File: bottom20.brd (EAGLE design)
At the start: 160 x 100 mm, 0 parts

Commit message: + bot.sch (Module verknüpfen + Anschluss)
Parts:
- added 5V-SCHALTREGLER1:C3: 100uF, 16V, ±20 %, iceberg20:CAPACITOR-THT-6.3
- added 5V-SCHALTREGLER1:C4: 1000uF, 25V, ±20 %, iceberg20:CAPACITOR-THT-10
- added 5V-SCHALTREGLER1:D1: 1N5822, iceberg20:DO-201AD
- added 5V-SCHALTREGLER1:IC2: LM2576, iceberg20:TO220-5PIN
- added 5V-SCHALTREGLER1:L1: L-100U, iceberg20:PISR
- added 5V-SCHALTREGLER1:R1: 100k, iceberg20:R0805
- added ANSCHLUSS1:CON1: Interface, iceberg20:CON-01X03
- added ANSCHLUSS1:X1: FTDI-Adapter, iceberg20:PIN-HEADER-ANGLED-6
- added ARDUINO1:C1, ARDUINO1:C5: 100nF, iceberg20:C0805
- added ARDUINO1:C2, ARDUINO1:C4: 1uF, iceberg20:C0805
- added ARDUINO1:C3: 4,7 µF, 16 V, ±20%, 3x5 mm, iceberg20:CAPACITOR-THT-3
- added ARDUINO1:IC1: ATMEGA328P-AU, iceberg20:ATMEGA328P-AU
- added ARDUINO1:Q1: 16MHz, iceberg20:CRYSTAL_HC49U-V
- added ARDUINO1:R1, ARDUINO1:R2: 1K, iceberg20:R0805
- added ARDUINO1:TP1: SCK, iceberg20:TESTPAD_B2,54
- added ARDUINO1:TP2: MISO, iceberg20:TESTPAD_B2,54
- added ARDUINO1:TP3: MOSI, iceberg20:TESTPAD_B2,54
- added ARDUINO1:TP4: SS, iceberg20:TESTPAD_B2,54
- added LED1:LED1, LED1:LED10, LED1:LED11, LED1:LED12, LED1:LED13, LED1:LED14, LED1:LED15, LED1:LED16, LED1:LED17, LED1:LED18, LED1:LED19, LED1:LED2, LED1:LED20, LED1:LED21, LED1:LED22, LED1:LED23, LED1:LED24, LED1:LED25, LED1:LED26, LED1:LED27, LED1:LED28, LED1:LED29, LED1:LED3, LED1:LED30, LED1:LED31, LED1:LED32, LED1:LED4, LED1:LED5, LED1:LED6, LED1:LED7, LED1:LED8, LED1:LED9: WS2812B, iceberg20:5050
- added PHOTOTRANSISTOR1:IC1, PHOTOTRANSISTOR2:IC1: MULTIPLEXER, iceberg20:SO24
- added PHOTOTRANSISTOR1:R1, PHOTOTRANSISTOR1:R10, PHOTOTRANSISTOR1:R11, PHOTOTRANSISTOR1:R12, PHOTOTRANSISTOR1:R13, PHOTOTRANSISTOR1:R14, PHOTOTRANSISTOR1:R15, PHOTOTRANSISTOR1:R16, PHOTOTRANSISTOR1:R2, PHOTOTRANSISTOR1:R3, PHOTOTRANSISTOR1:R4, PHOTOTRANSISTOR1:R5, PHOTOTRANSISTOR1:R6, PHOTOTRANSISTOR1:R7, PHOTOTRANSISTOR1:R8, PHOTOTRANSISTOR1:R9, PHOTOTRANSISTOR2:R1, PHOTOTRANSISTOR2:R10, PHOTOTRANSISTOR2:R11, PHOTOTRANSISTOR2:R12, PHOTOTRANSISTOR2:R13, PHOTOTRANSISTOR2:R14, PHOTOTRANSISTOR2:R15, PHOTOTRANSISTOR2:R16, PHOTOTRANSISTOR2:R2, PHOTOTRANSISTOR2:R3, PHOTOTRANSISTOR2:R4, PHOTOTRANSISTOR2:R5, PHOTOTRANSISTOR2:R6, PHOTOTRANSISTOR2:R7, PHOTOTRANSISTOR2:R8, PHOTOTRANSISTOR2:R9: R, iceberg20:R0805
- added PHOTOTRANSISTOR1:T1, PHOTOTRANSISTOR1:T10, PHOTOTRANSISTOR1:T11, PHOTOTRANSISTOR1:T12, PHOTOTRANSISTOR1:T13, PHOTOTRANSISTOR1:T14, PHOTOTRANSISTOR1:T15, PHOTOTRANSISTOR1:T16, PHOTOTRANSISTOR1:T2, PHOTOTRANSISTOR1:T3, PHOTOTRANSISTOR1:T4, PHOTOTRANSISTOR1:T5, PHOTOTRANSISTOR1:T6, PHOTOTRANSISTOR1:T7, PHOTOTRANSISTOR1:T8, PHOTOTRANSISTOR1:T9, PHOTOTRANSISTOR2:T1, PHOTOTRANSISTOR2:T10, PHOTOTRANSISTOR2:T11, PHOTOTRANSISTOR2:T12, PHOTOTRANSISTOR2:T13, PHOTOTRANSISTOR2:T14, PHOTOTRANSISTOR2:T15, PHOTOTRANSISTOR2:T16, PHOTOTRANSISTOR2:T2, PHOTOTRANSISTOR2:T3, PHOTOTRANSISTOR2:T4, PHOTOTRANSISTOR2:T5, PHOTOTRANSISTOR2:T6, PHOTOTRANSISTOR2:T7, PHOTOTRANSISTOR2:T8, PHOTOTRANSISTOR2:T9: SFH320, iceberg20:PLCC-2
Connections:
- new net +12V: 5V-SCHALTREGLER1:C3.1, 5V-SCHALTREGLER1:IC2.1, ANSCHLUSS1:CON1.3
- new net +5V: 5V-SCHALTREGLER1:C4.1, 5V-SCHALTREGLER1:IC2.4, 5V-SCHALTREGLER1:L1.2, 5V-SCHALTREGLER1:R1.2, ARDUINO1:C2.1, ARDUINO1:C3.1, ARDUINO1:C4.1, ARDUINO1:IC1.18, ARDUINO1:IC1.4, ARDUINO1:IC1.6, LED1:LED1.VDD, LED1:LED10.VDD, LED1:LED11.VDD, LED1:LED12.VDD, LED1:LED13.VDD, LED1:LED14.VDD, LED1:LED15.VDD, LED1:LED16.VDD, LED1:LED17.VDD, LED1:LED18.VDD, LED1:LED19.VDD, LED1:LED2.VDD, LED1:LED20.VDD, LED1:LED21.VDD, LED1:LED22.VDD, LED1:LED23.VDD, LED1:LED24.VDD, LED1:LED25.VDD, LED1:LED26.VDD, LED1:LED27.VDD, LED1:LED28.VDD, LED1:LED29.VDD, LED1:LED3.VDD, LED1:LED30.VDD, LED1:LED31.VDD, LED1:LED32.VDD, LED1:LED4.VDD, LED1:LED5.VDD, LED1:LED6.VDD, LED1:LED7.VDD, LED1:LED8.VDD, LED1:LED9.VDD, PHOTOTRANSISTOR1:IC1.24, PHOTOTRANSISTOR1:R1.2, PHOTOTRANSISTOR1:R10.2, PHOTOTRANSISTOR1:R11.2, PHOTOTRANSISTOR1:R12.2, PHOTOTRANSISTOR1:R13.2, PHOTOTRANSISTOR1:R14.2, PHOTOTRANSISTOR1:R15.2, PHOTOTRANSISTOR1:R16.2, PHOTOTRANSISTOR1:R2.2, PHOTOTRANSISTOR1:R3.2, PHOTOTRANSISTOR1:R4.2, PHOTOTRANSISTOR1:R5.2, PHOTOTRANSISTOR1:R6.2, PHOTOTRANSISTOR1:R7.2, PHOTOTRANSISTOR1:R8.2, PHOTOTRANSISTOR1:R9.2, PHOTOTRANSISTOR2:IC1.24, PHOTOTRANSISTOR2:R1.2, PHOTOTRANSISTOR2:R10.2, PHOTOTRANSISTOR2:R11.2, PHOTOTRANSISTOR2:R12.2, PHOTOTRANSISTOR2:R13.2, PHOTOTRANSISTOR2:R14.2, PHOTOTRANSISTOR2:R15.2, PHOTOTRANSISTOR2:R16.2, PHOTOTRANSISTOR2:R2.2, PHOTOTRANSISTOR2:R3.2, PHOTOTRANSISTOR2:R4.2, PHOTOTRANSISTOR2:R5.2, PHOTOTRANSISTOR2:R6.2, PHOTOTRANSISTOR2:R7.2, PHOTOTRANSISTOR2:R8.2, PHOTOTRANSISTOR2:R9.2
- new net 5V-SCHALTREGLER1:N$1: 5V-SCHALTREGLER1:IC2.5, 5V-SCHALTREGLER1:R1.1
- new net 5V-SCHALTREGLER1:N$2: 5V-SCHALTREGLER1:D1.1, 5V-SCHALTREGLER1:IC2.2, 5V-SCHALTREGLER1:L1.1
- new net ANSCHLUSS1:CTS: ANSCHLUSS1:X1.P$2
- new net ANSCHLUSS1:DTR: ANSCHLUSS1:X1.P$6
- new net ANSCHLUSS1:RX: ANSCHLUSS1:X1.P$5
- new net ANSCHLUSS1:TX: ANSCHLUSS1:X1.P$4
- new net ARDUINO1:A1: ARDUINO1:IC1.24
- new net ARDUINO1:A2: ARDUINO1:IC1.25
- new net ARDUINO1:A3: ARDUINO1:IC1.26
- new net ARDUINO1:ADC6: ARDUINO1:IC1.19
- new net ARDUINO1:ADC7: ARDUINO1:IC1.22
- new net ARDUINO1:AIN0: ARDUINO1:IC1.10
- new net ARDUINO1:AIN1: ARDUINO1:IC1.11
- new net ARDUINO1:AO: ARDUINO1:IC1.23
- new net ARDUINO1:ARDUINO-RESET: ARDUINO1:C1.1
- new net ARDUINO1:D10: ARDUINO1:IC1.14, ARDUINO1:TP4.TP
- new net ARDUINO1:D4: ARDUINO1:IC1.2
- new net ARDUINO1:D5: ARDUINO1:IC1.9
- new net ARDUINO1:D8: ARDUINO1:IC1.12
- new net ARDUINO1:D9: ARDUINO1:IC1.13
- new net ARDUINO1:INT0: ARDUINO1:IC1.1
- new net ARDUINO1:INT1: ARDUINO1:IC1.32
- new net ARDUINO1:N$1: ARDUINO1:C1.2, ARDUINO1:IC1.29
- new net ARDUINO1:N$12: ARDUINO1:IC1.30, ARDUINO1:R1.1
- new net ARDUINO1:N$13: ARDUINO1:IC1.31, ARDUINO1:R2.1
- new net ARDUINO1:N$5: ARDUINO1:IC1.15, ARDUINO1:TP3.TP
- new net ARDUINO1:N$6: ARDUINO1:IC1.16, ARDUINO1:TP2.TP
- new net ARDUINO1:N$7: ARDUINO1:IC1.17, ARDUINO1:TP1.TP
- new net ARDUINO1:N$8: ARDUINO1:C5.1, ARDUINO1:IC1.20
- new net ARDUINO1:SCL: ARDUINO1:IC1.28
- new net ARDUINO1:SDA: ARDUINO1:IC1.27
- new net GND: 5V-SCHALTREGLER1:C3.2, 5V-SCHALTREGLER1:C4.2, 5V-SCHALTREGLER1:D1.2, 5V-SCHALTREGLER1:IC2.3, ANSCHLUSS1:X1.P$1, ARDUINO1:C2.2, ARDUINO1:C3.2, ARDUINO1:C4.2, ARDUINO1:C5.2, ARDUINO1:IC1.21, ARDUINO1:IC1.3, ARDUINO1:IC1.5, ARDUINO1:IC1.7, ARDUINO1:IC1.8, ARDUINO1:Q1.1, ARDUINO1:Q1.2, LED1:LED1.GND, LED1:LED10.GND, LED1:LED11.GND, LED1:LED12.GND, LED1:LED13.GND, LED1:LED14.GND, LED1:LED15.GND, LED1:LED16.GND, LED1:LED17.GND, LED1:LED18.GND, LED1:LED19.GND, LED1:LED2.GND, LED1:LED20.GND, LED1:LED21.GND, LED1:LED22.GND, LED1:LED23.GND, LED1:LED24.GND, LED1:LED25.GND, LED1:LED26.GND, LED1:LED27.GND, LED1:LED28.GND, LED1:LED29.GND, LED1:LED3.GND, LED1:LED30.GND, LED1:LED31.GND, LED1:LED32.GND, LED1:LED4.GND, LED1:LED5.GND, LED1:LED6.GND, LED1:LED7.GND, LED1:LED8.GND, LED1:LED9.GND
- new net LED-IN: LED1:LED1.IN
- new net LED1:CON-1: LED1:LED8.OUT, LED1:LED9.IN
- new net LED1:CON-2: LED1:LED16.OUT, LED1:LED17.IN
- new net LED1:CON-3: LED1:LED24.OUT, LED1:LED25.IN
- new net LED1:LED-IN1: LED1:LED2.OUT, LED1:LED3.IN
- new net LED1:LED-IN10: LED1:LED20.OUT, LED1:LED21.IN
- new net LED1:LED-IN11: LED1:LED22.OUT, LED1:LED23.IN
- new net LED1:LED-IN12: LED1:LED30.OUT, LED1:LED31.IN
- new net LED1:LED-IN2: LED1:LED4.OUT, LED1:LED5.IN
- new net LED1:LED-IN3: LED1:LED6.OUT, LED1:LED7.IN
- new net LED1:LED-IN4: LED1:LED26.OUT, LED1:LED27.IN
- new net LED1:LED-IN5: LED1:LED10.OUT, LED1:LED11.IN
- new net LED1:LED-IN6: LED1:LED12.OUT, LED1:LED13.IN
- new net LED1:LED-IN7: LED1:LED14.OUT, LED1:LED15.IN
- new net LED1:LED-IN8: LED1:LED28.OUT, LED1:LED29.IN
- new net LED1:LED-IN9: LED1:LED18.OUT, LED1:LED19.IN
- new net LED1:N$1: LED1:LED3.OUT, LED1:LED4.IN
- new net LED1:N$11: LED1:LED11.OUT, LED1:LED12.IN
- new net LED1:N$12: LED1:LED13.OUT, LED1:LED14.IN
- new net LED1:N$13: LED1:LED15.OUT, LED1:LED16.IN
- new net LED1:N$14: LED1:LED17.OUT, LED1:LED18.IN
- new net LED1:N$16: LED1:LED19.OUT, LED1:LED20.IN
- new net LED1:N$17: LED1:LED21.OUT, LED1:LED22.IN
- new net LED1:N$18: LED1:LED23.OUT, LED1:LED24.IN
- new net LED1:N$2: LED1:LED1.OUT, LED1:LED2.IN
- new net LED1:N$3: LED1:LED25.OUT, LED1:LED26.IN
- new net LED1:N$4: LED1:LED5.OUT, LED1:LED6.IN
- new net LED1:N$5: LED1:LED27.OUT, LED1:LED28.IN
- new net LED1:N$6: LED1:LED29.OUT, LED1:LED30.IN
- new net LED1:N$7: LED1:LED7.OUT, LED1:LED8.IN
- new net LED1:N$8: LED1:LED31.OUT, LED1:LED32.IN
- new net LED1:N$9: LED1:LED10.IN, LED1:LED9.OUT
- new net N$2: ANSCHLUSS1:CON1.2, ARDUINO1:R1.2
- new net N$3: ANSCHLUSS1:CON1.1, ARDUINO1:R2.2
- new net N$6: ANSCHLUSS1:X1.P$3
- new net PHOTOTRANSISTOR1:BIT0: PHOTOTRANSISTOR1:IC1.11
- new net PHOTOTRANSISTOR1:BIT1: PHOTOTRANSISTOR1:IC1.10
- new net PHOTOTRANSISTOR1:BIT2: PHOTOTRANSISTOR1:IC1.14
- new net PHOTOTRANSISTOR1:BIT3: PHOTOTRANSISTOR1:IC1.13
- new net PHOTOTRANSISTOR1:GND: PHOTOTRANSISTOR1:IC1.12, PHOTOTRANSISTOR1:T1.C, PHOTOTRANSISTOR1:T10.C, PHOTOTRANSISTOR1:T11.C, PHOTOTRANSISTOR1:T12.C, PHOTOTRANSISTOR1:T13.C, PHOTOTRANSISTOR1:T14.C, PHOTOTRANSISTOR1:T15.C, PHOTOTRANSISTOR1:T16.C, PHOTOTRANSISTOR1:T2.C, PHOTOTRANSISTOR1:T3.C, PHOTOTRANSISTOR1:T4.C, PHOTOTRANSISTOR1:T5.C, PHOTOTRANSISTOR1:T6.C, PHOTOTRANSISTOR1:T7.C, PHOTOTRANSISTOR1:T8.C, PHOTOTRANSISTOR1:T9.C
- new net PHOTOTRANSISTOR1:MULTIPLEXER-ENABLE: PHOTOTRANSISTOR1:IC1.15
- new net PHOTOTRANSISTOR1:N$1: PHOTOTRANSISTOR1:IC1.9, PHOTOTRANSISTOR1:R1.1, PHOTOTRANSISTOR1:T1.A
- new net PHOTOTRANSISTOR1:N$10: PHOTOTRANSISTOR1:IC1.3, PHOTOTRANSISTOR1:R7.1, PHOTOTRANSISTOR1:T7.A
- new net PHOTOTRANSISTOR1:N$11: PHOTOTRANSISTOR1:IC1.4, PHOTOTRANSISTOR1:R6.1, PHOTOTRANSISTOR1:T6.A
- new net PHOTOTRANSISTOR1:N$12: PHOTOTRANSISTOR1:IC1.17, PHOTOTRANSISTOR1:R10.1, PHOTOTRANSISTOR1:T10.A
- new net PHOTOTRANSISTOR1:N$14: PHOTOTRANSISTOR1:IC1.18, PHOTOTRANSISTOR1:R11.1, PHOTOTRANSISTOR1:T11.A
- new net PHOTOTRANSISTOR1:N$18: PHOTOTRANSISTOR1:IC1.20, PHOTOTRANSISTOR1:R13.1, PHOTOTRANSISTOR1:T13.A
- new net PHOTOTRANSISTOR1:N$2: PHOTOTRANSISTOR1:IC1.8, PHOTOTRANSISTOR1:R2.1, PHOTOTRANSISTOR1:T2.A
- new net PHOTOTRANSISTOR1:N$20: PHOTOTRANSISTOR1:IC1.21, PHOTOTRANSISTOR1:R14.1, PHOTOTRANSISTOR1:T14.A
- new net PHOTOTRANSISTOR1:N$22: PHOTOTRANSISTOR1:IC1.22, PHOTOTRANSISTOR1:R15.1, PHOTOTRANSISTOR1:T15.A
- new net PHOTOTRANSISTOR1:N$25: PHOTOTRANSISTOR1:IC1.23, PHOTOTRANSISTOR1:R16.1, PHOTOTRANSISTOR1:T16.A
- new net PHOTOTRANSISTOR1:N$26: PHOTOTRANSISTOR1:IC1.19, PHOTOTRANSISTOR1:R12.1, PHOTOTRANSISTOR1:T12.A
- new net PHOTOTRANSISTOR1:N$3: PHOTOTRANSISTOR1:IC1.7, PHOTOTRANSISTOR1:R3.1, PHOTOTRANSISTOR1:T3.A
- new net PHOTOTRANSISTOR1:N$4: PHOTOTRANSISTOR1:IC1.6, PHOTOTRANSISTOR1:R4.1, PHOTOTRANSISTOR1:T4.A
- new net PHOTOTRANSISTOR1:N$5: PHOTOTRANSISTOR1:IC1.5, PHOTOTRANSISTOR1:R5.1, PHOTOTRANSISTOR1:T5.A
- new net PHOTOTRANSISTOR1:N$7: PHOTOTRANSISTOR1:IC1.16, PHOTOTRANSISTOR1:R9.1, PHOTOTRANSISTOR1:T9.A
- new net PHOTOTRANSISTOR1:N$9: PHOTOTRANSISTOR1:IC1.2, PHOTOTRANSISTOR1:R8.1, PHOTOTRANSISTOR1:T8.A
- new net PHOTOTRANSISTOR1:TRANSISTOR-SIGNAL: PHOTOTRANSISTOR1:IC1.1
- new net PHOTOTRANSISTOR2:BIT0: PHOTOTRANSISTOR2:IC1.11
- new net PHOTOTRANSISTOR2:BIT1: PHOTOTRANSISTOR2:IC1.10
- new net PHOTOTRANSISTOR2:BIT2: PHOTOTRANSISTOR2:IC1.14
- new net PHOTOTRANSISTOR2:BIT3: PHOTOTRANSISTOR2:IC1.13
- new net PHOTOTRANSISTOR2:GND: PHOTOTRANSISTOR2:IC1.12, PHOTOTRANSISTOR2:T1.C, PHOTOTRANSISTOR2:T10.C, PHOTOTRANSISTOR2:T11.C, PHOTOTRANSISTOR2:T12.C, PHOTOTRANSISTOR2:T13.C, PHOTOTRANSISTOR2:T14.C, PHOTOTRANSISTOR2:T15.C, PHOTOTRANSISTOR2:T16.C, PHOTOTRANSISTOR2:T2.C, PHOTOTRANSISTOR2:T3.C, PHOTOTRANSISTOR2:T4.C, PHOTOTRANSISTOR2:T5.C, PHOTOTRANSISTOR2:T6.C, PHOTOTRANSISTOR2:T7.C, PHOTOTRANSISTOR2:T8.C, PHOTOTRANSISTOR2:T9.C
- new net PHOTOTRANSISTOR2:MULTIPLEXER-ENABLE: PHOTOTRANSISTOR2:IC1.15
- new net PHOTOTRANSISTOR2:N$1: PHOTOTRANSISTOR2:IC1.9, PHOTOTRANSISTOR2:R1.1, PHOTOTRANSISTOR2:T1.A
- new net PHOTOTRANSISTOR2:N$10: PHOTOTRANSISTOR2:IC1.3, PHOTOTRANSISTOR2:R7.1, PHOTOTRANSISTOR2:T7.A
- new net PHOTOTRANSISTOR2:N$11: PHOTOTRANSISTOR2:IC1.4, PHOTOTRANSISTOR2:R6.1, PHOTOTRANSISTOR2:T6.A
- new net PHOTOTRANSISTOR2:N$12: PHOTOTRANSISTOR2:IC1.17, PHOTOTRANSISTOR2:R10.1, PHOTOTRANSISTOR2:T10.A
- new net PHOTOTRANSISTOR2:N$14: PHOTOTRANSISTOR2:IC1.18, PHOTOTRANSISTOR2:R11.1, PHOTOTRANSISTOR2:T11.A
- new net PHOTOTRANSISTOR2:N$18: PHOTOTRANSISTOR2:IC1.20, PHOTOTRANSISTOR2:R13.1, PHOTOTRANSISTOR2:T13.A
- new net PHOTOTRANSISTOR2:N$2: PHOTOTRANSISTOR2:IC1.8, PHOTOTRANSISTOR2:R2.1, PHOTOTRANSISTOR2:T2.A
- new net PHOTOTRANSISTOR2:N$20: PHOTOTRANSISTOR2:IC1.21, PHOTOTRANSISTOR2:R14.1, PHOTOTRANSISTOR2:T14.A
- new net PHOTOTRANSISTOR2:N$22: PHOTOTRANSISTOR2:IC1.22, PHOTOTRANSISTOR2:R15.1, PHOTOTRANSISTOR2:T15.A
- new net PHOTOTRANSISTOR2:N$25: PHOTOTRANSISTOR2:IC1.23, PHOTOTRANSISTOR2:R16.1, PHOTOTRANSISTOR2:T16.A
- new net PHOTOTRANSISTOR2:N$26: PHOTOTRANSISTOR2:IC1.19, PHOTOTRANSISTOR2:R12.1, PHOTOTRANSISTOR2:T12.A
- new net PHOTOTRANSISTOR2:N$3: PHOTOTRANSISTOR2:IC1.7, PHOTOTRANSISTOR2:R3.1, PHOTOTRANSISTOR2:T3.A
- new net PHOTOTRANSISTOR2:N$4: PHOTOTRANSISTOR2:IC1.6, PHOTOTRANSISTOR2:R4.1, PHOTOTRANSISTOR2:T4.A
- new net PHOTOTRANSISTOR2:N$5: PHOTOTRANSISTOR2:IC1.5, PHOTOTRANSISTOR2:R5.1, PHOTOTRANSISTOR2:T5.A
- new net PHOTOTRANSISTOR2:N$7: PHOTOTRANSISTOR2:IC1.16, PHOTOTRANSISTOR2:R9.1, PHOTOTRANSISTOR2:T9.A
- new net PHOTOTRANSISTOR2:N$9: PHOTOTRANSISTOR2:IC1.2, PHOTOTRANSISTOR2:R8.1, PHOTOTRANSISTOR2:T8.A
- new net PHOTOTRANSISTOR2:TRANSISTOR-SIGNAL: PHOTOTRANSISTOR2:IC1.1

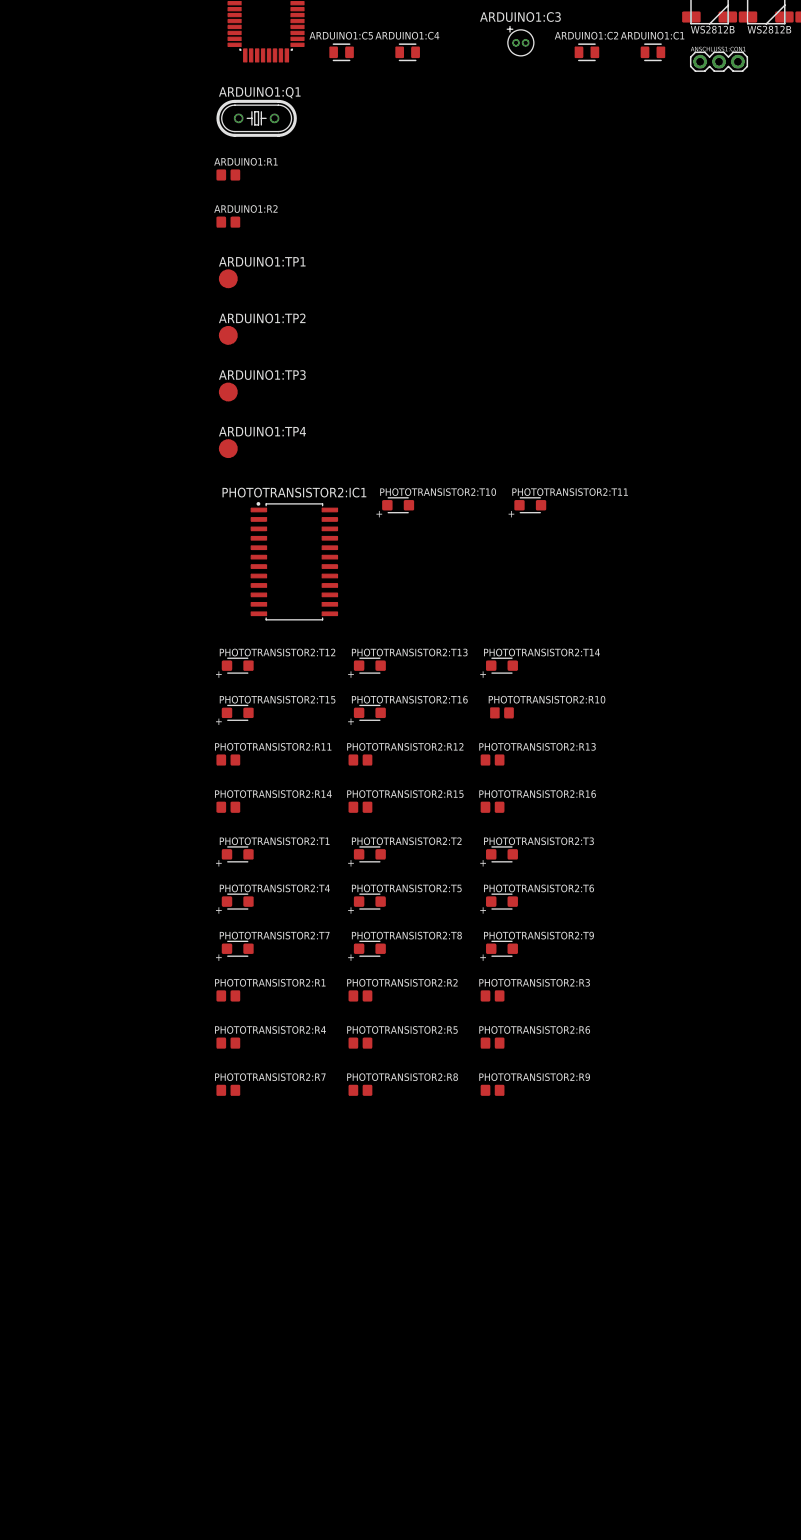
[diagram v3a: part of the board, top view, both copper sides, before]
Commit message: - bot.sch ( Anschluss)
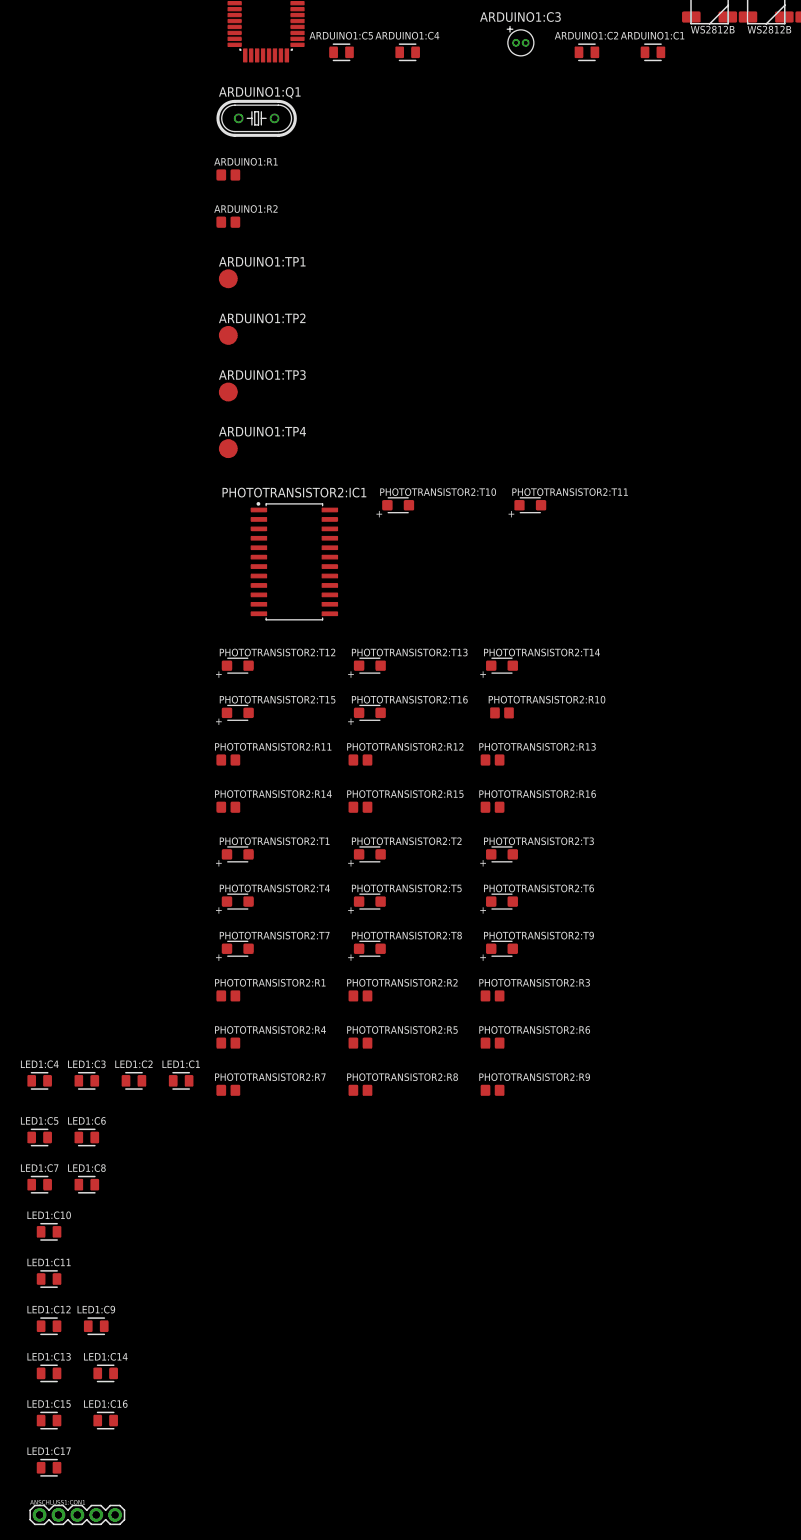
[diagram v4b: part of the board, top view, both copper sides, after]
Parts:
- added LED1:C1, LED1:C10, LED1:C11, LED1:C12, LED1:C13, LED1:C14, LED1:C15, LED1:C16, LED1:C17, LED1:C2, LED1:C3, LED1:C4, LED1:C5, LED1:C6, LED1:C7, LED1:C8, LED1:C9: C0805, iceberg20:C0805
- ANSCHLUSS1:CON1: value Interface -> HOLE-01X05; device iceberg20:CON-01X03 -> iceberg20:5X1
- moved ANSCHLUSS1:CON1 214.8 mm to (-1167.1, -487.7)
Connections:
- new net ANSCHLUSS1:LED-IN: ANSCHLUSS1:CON1.3
- net +12V: now also ANSCHLUSS1:CON1.5; no longer ANSCHLUSS1:CON1.3
- net +5V: now also LED1:C1.1, LED1:C10.1, LED1:C11.1, LED1:C12.1, LED1:C13.1, LED1:C14.1, LED1:C15.1, LED1:C16.1, LED1:C17.1, LED1:C2.1, LED1:C3.1, LED1:C4.1, LED1:C5.1, LED1:C6.1, LED1:C7.1, LED1:C8.1, LED1:C9.1
- net GND: now also ANSCHLUSS1:CON1.4, LED1:C1.2, LED1:C10.2, LED1:C11.2, LED1:C12.2, LED1:C13.2, LED1:C14.2, LED1:C15.2, LED1:C16.2, LED1:C17.2, LED1:C2.2, LED1:C3.2, LED1:C4.2, LED1:C5.2, LED1:C6.2, LED1:C7.2, LED1:C8.2, LED1:C9.2

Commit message: - bot.sch (Übersicht, Anschluss)
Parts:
- removed ANSCHLUSS1:CON1: HOLE-01X05, iceberg20:5X1
- added ANSCHLUSS1:X2: CON-UP, iceberg20:PIN-HEADER-ANGLED-6
- added ARDUINO1:C6, ARDUINO1:C7: 15p, iceberg20:C0805
- added ARDUINO1:R3: R, iceberg20:R0805
- added ARDUINO1:R4: 1k, iceberg20:R0805
- added ARDUINO1:S1: SMD-BUTTON, iceberg20:SWITCH-6MM-SMD
- ARDUINO1:C1, ARDUINO1:C5: value 100nF -> 100n
- ARDUINO1:C2, ARDUINO1:C4: value 1uF -> 1u
- ARDUINO1:C3: value 4,7 µF, 16 V, ±20%, 3x5 mm -> 4,7u, 16V
- ARDUINO1:R1, ARDUINO1:R2: value 1K -> 1k
- LED1:C1, LED1:C10, LED1:C11, LED1:C12, LED1:C13, LED1:C14, LED1:C15, LED1:C16, LED1:C17, LED1:C2, LED1:C3, LED1:C4, LED1:C5, LED1:C6, LED1:C7, LED1:C8, LED1:C9: value C0805 -> 100n
- PHOTOTRANSISTOR1:R1, PHOTOTRANSISTOR1:R10, PHOTOTRANSISTOR1:R11, PHOTOTRANSISTOR1:R12, PHOTOTRANSISTOR1:R13, PHOTOTRANSISTOR1:R14, PHOTOTRANSISTOR1:R15, PHOTOTRANSISTOR1:R16, PHOTOTRANSISTOR1:R2, PHOTOTRANSISTOR1:R3, PHOTOTRANSISTOR1:R4, PHOTOTRANSISTOR1:R5, PHOTOTRANSISTOR1:R6, PHOTOTRANSISTOR1:R7, PHOTOTRANSISTOR1:R8, PHOTOTRANSISTOR1:R9, PHOTOTRANSISTOR2:R1, PHOTOTRANSISTOR2:R10, PHOTOTRANSISTOR2:R11, PHOTOTRANSISTOR2:R12, PHOTOTRANSISTOR2:R13, PHOTOTRANSISTOR2:R14, PHOTOTRANSISTOR2:R15, PHOTOTRANSISTOR2:R16, PHOTOTRANSISTOR2:R2, PHOTOTRANSISTOR2:R3, PHOTOTRANSISTOR2:R4, PHOTOTRANSISTOR2:R5, PHOTOTRANSISTOR2:R6, PHOTOTRANSISTOR2:R7, PHOTOTRANSISTOR2:R8, PHOTOTRANSISTOR2:R9: value R -> 20k
- moved ANSCHLUSS1:X1 1315.9 mm to (-1244.6, -569.0)
- moved ARDUINO1:TP1 507.9 mm to (-1437.6, -734.1)
- moved ARDUINO1:TP2 507.9 mm to (-1437.6, -741.7)
- moved ARDUINO1:TP3 507.9 mm to (-1437.6, -749.3)
- moved ARDUINO1:TP4 507.9 mm to (-1437.6, -756.9)
- moved ARDUINO1:R1 489.5 mm to (-1437.6, -697.2)
- moved ARDUINO1:R2 489.5 mm to (-1437.6, -703.6)
- moved ARDUINO1:Q1 489.5 mm to (-1433.8, -689.6)
- moved ARDUINO1:IC1 488.5 mm to (-1432.6, -675.6)
- moved ARDUINO1:C3 481.9 mm to (-1385.6, -679.5)
- moved ARDUINO1:C1 480.9 mm to (-1367.8, -679.5)
- moved ARDUINO1:C2 480.9 mm to (-1376.7, -679.5)
- moved ARDUINO1:C4 477.9 mm to (-1395.7, -679.5)
- moved ARDUINO1:C5 477.9 mm to (-1404.6, -679.5)
- moved PHOTOTRANSISTOR2:T11 373.9 mm to (-1278.9, -680.7)
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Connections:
- net ANSCHLUSS1:CTS renamed N$10
- net ARDUINO1:A1 renamed BITA1
- net ARDUINO1:A2 renamed BITA2
- net ARDUINO1:A3 renamed BITA3
- net ARDUINO1:AO renamed BITA0
- net ARDUINO1:D4 renamed BITB0
- net ARDUINO1:D5 renamed BITB1
- net ARDUINO1:D8 renamed BITB2
- net ARDUINO1:D9 renamed BITB3
- net N$6 renamed ANSCHLUSS1:VID
- removed net ANSCHLUSS1:DTR: ANSCHLUSS1:X1.P$6
- removed net ANSCHLUSS1:LED-IN: ANSCHLUSS1:CON1.3
- removed net ANSCHLUSS1:RX: ANSCHLUSS1:X1.P$5
- removed net ANSCHLUSS1:TX: ANSCHLUSS1:X1.P$4
- removed net ARDUINO1:ADC6: ARDUINO1:IC1.19
- removed net ARDUINO1:ADC7: ARDUINO1:IC1.22
- removed net ARDUINO1:AIN0: ARDUINO1:IC1.10
- removed net ARDUINO1:ARDUINO-RESET: ARDUINO1:C1.1
- removed net ARDUINO1:INT0: ARDUINO1:IC1.1
- removed net ARDUINO1:INT1: ARDUINO1:IC1.32
- removed net ARDUINO1:SCL: ARDUINO1:IC1.28
- removed net ARDUINO1:SDA: ARDUINO1:IC1.27
- removed net N$3: ANSCHLUSS1:CON1.1, ARDUINO1:R2.2
- removed net PHOTOTRANSISTOR1:GND: PHOTOTRANSISTOR1:IC1.12, PHOTOTRANSISTOR1:T1.C, PHOTOTRANSISTOR1:T10.C, PHOTOTRANSISTOR1:T11.C, PHOTOTRANSISTOR1:T12.C, PHOTOTRANSISTOR1:T13.C, PHOTOTRANSISTOR1:T14.C, PHOTOTRANSISTOR1:T15.C, PHOTOTRANSISTOR1:T16.C, PHOTOTRANSISTOR1:T2.C, PHOTOTRANSISTOR1:T3.C, PHOTOTRANSISTOR1:T4.C, PHOTOTRANSISTOR1:T5.C, PHOTOTRANSISTOR1:T6.C, PHOTOTRANSISTOR1:T7.C, PHOTOTRANSISTOR1:T8.C, PHOTOTRANSISTOR1:T9.C
- removed net PHOTOTRANSISTOR1:MULTIPLEXER-ENABLE: PHOTOTRANSISTOR1:IC1.15
- removed net PHOTOTRANSISTOR1:TRANSISTOR-SIGNAL: PHOTOTRANSISTOR1:IC1.1
- removed net PHOTOTRANSISTOR2:GND: PHOTOTRANSISTOR2:IC1.12, PHOTOTRANSISTOR2:T1.C, PHOTOTRANSISTOR2:T10.C, PHOTOTRANSISTOR2:T11.C, PHOTOTRANSISTOR2:T12.C, PHOTOTRANSISTOR2:T13.C, PHOTOTRANSISTOR2:T14.C, PHOTOTRANSISTOR2:T15.C, PHOTOTRANSISTOR2:T16.C, PHOTOTRANSISTOR2:T2.C, PHOTOTRANSISTOR2:T3.C, PHOTOTRANSISTOR2:T4.C, PHOTOTRANSISTOR2:T5.C, PHOTOTRANSISTOR2:T6.C, PHOTOTRANSISTOR2:T7.C, PHOTOTRANSISTOR2:T8.C, PHOTOTRANSISTOR2:T9.C
- removed net PHOTOTRANSISTOR2:MULTIPLEXER-ENABLE: PHOTOTRANSISTOR2:IC1.15
- removed net PHOTOTRANSISTOR2:TRANSISTOR-SIGNAL: PHOTOTRANSISTOR2:IC1.1
- new net 5V-SCHALTREGLER1:GND: 5V-SCHALTREGLER1:C3.2, 5V-SCHALTREGLER1:C4.2, 5V-SCHALTREGLER1:D1.2, 5V-SCHALTREGLER1:IC2.3
- new net ANSCHLUSS1:N$1: ANSCHLUSS1:X2.P$5
- new net ARD-IN: ANSCHLUSS1:X2.P$1, ARDUINO1:IC1.10
- new net ARD-RST: ANSCHLUSS1:X1.P$6, ARDUINO1:C1.1
- new net ARDUINO1:N$2: ARDUINO1:C7.1, ARDUINO1:IC1.8, ARDUINO1:Q1.1
- new net ARDUINO1:N$3: ARDUINO1:C6.2, ARDUINO1:IC1.7, ARDUINO1:Q1.2
- new net BIT0: PHOTOTRANSISTOR2:IC1.11
- new net BIT1: PHOTOTRANSISTOR2:IC1.10
- new net BIT2: PHOTOTRANSISTOR2:IC1.14
- new net BIT3: PHOTOTRANSISTOR2:IC1.13
- new net N$1: ANSCHLUSS1:X2.P$6
- new net N$4: ARDUINO1:IC1.1, PHOTOTRANSISTOR2:IC1.15
- new net N$5: ARDUINO1:C2.1, ARDUINO1:C3.1, ARDUINO1:C4.1, ARDUINO1:IC1.18, ARDUINO1:IC1.4, ARDUINO1:IC1.6, ARDUINO1:R3.2
- new net N$6: ARDUINO1:IC1.19, PHOTOTRANSISTOR1:IC1.15
- new net N$7: ARDUINO1:IC1.22, PHOTOTRANSISTOR1:IC1.1
- new net RX: ANSCHLUSS1:X1.P$5, ARDUINO1:R2.2
- new net SCL: ANSCHLUSS1:X2.P$3, ARDUINO1:IC1.28
- new net SDA: ANSCHLUSS1:X2.P$2, ARDUINO1:IC1.27
- new net TX: ANSCHLUSS1:X1.P$4, ARDUINO1:R1.2
- net +12V: no longer ANSCHLUSS1:CON1.5
- net +5V: no longer ARDUINO1:C2.1, ARDUINO1:C3.1, ARDUINO1:C4.1, ARDUINO1:IC1.18, ARDUINO1:IC1.4, ARDUINO1:IC1.6
- net ARDUINO1:N$1: now also ARDUINO1:R3.1, ARDUINO1:S1.A1, ARDUINO1:S1.A2
- net GND: now also ARDUINO1:C6.1, ARDUINO1:C7.2, ARDUINO1:R4.1, ARDUINO1:R4.2, ARDUINO1:S1.B1, ARDUINO1:S1.B2, PHOTOTRANSISTOR1:IC1.12, PHOTOTRANSISTOR1:T1.C, PHOTOTRANSISTOR1:T10.C, PHOTOTRANSISTOR1:T11.C, PHOTOTRANSISTOR1:T12.C, PHOTOTRANSISTOR1:T13.C, PHOTOTRANSISTOR1:T14.C, PHOTOTRANSISTOR1:T15.C, PHOTOTRANSISTOR1:T16.C, PHOTOTRANSISTOR1:T2.C, PHOTOTRANSISTOR1:T3.C, PHOTOTRANSISTOR1:T4.C, PHOTOTRANSISTOR1:T5.C, PHOTOTRANSISTOR1:T6.C, PHOTOTRANSISTOR1:T7.C, PHOTOTRANSISTOR1:T8.C, PHOTOTRANSISTOR1:T9.C, PHOTOTRANSISTOR2:IC1.12, PHOTOTRANSISTOR2:T1.C, PHOTOTRANSISTOR2:T10.C, PHOTOTRANSISTOR2:T11.C, PHOTOTRANSISTOR2:T12.C, PHOTOTRANSISTOR2:T13.C, PHOTOTRANSISTOR2:T14.C, PHOTOTRANSISTOR2:T15.C, PHOTOTRANSISTOR2:T16.C, PHOTOTRANSISTOR2:T2.C, PHOTOTRANSISTOR2:T3.C, PHOTOTRANSISTOR2:T4.C, PHOTOTRANSISTOR2:T5.C, PHOTOTRANSISTOR2:T6.C, PHOTOTRANSISTOR2:T7.C, PHOTOTRANSISTOR2:T8.C, PHOTOTRANSISTOR2:T9.C; no longer 5V-SCHALTREGLER1:C3.2, 5V-SCHALTREGLER1:C4.2, 5V-SCHALTREGLER1:D1.2, 5V-SCHALTREGLER1:IC2.3, ANSCHLUSS1:CON1.4, ARDUINO1:IC1.7, ARDUINO1:IC1.8, ARDUINO1:Q1.1, ARDUINO1:Q1.2
- net LED-IN: now also ANSCHLUSS1:X2.P$4
- net N$2: now also ARDUINO1:IC1.32, PHOTOTRANSISTOR2:IC1.1; no longer ANSCHLUSS1:CON1.2, ARDUINO1:R1.2

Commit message: - bot.sch (Übersicht)
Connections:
- removed net 5V-SCHALTREGLER1:GND: 5V-SCHALTREGLER1:C3.2, 5V-SCHALTREGLER1:C4.2, 5V-SCHALTREGLER1:D1.2, 5V-SCHALTREGLER1:IC2.3
- removed net ANSCHLUSS1:VID: ANSCHLUSS1:X1.P$3
- net +5V: now also ANSCHLUSS1:X1.P$3
- net GND: now also 5V-SCHALTREGLER1:C3.2, 5V-SCHALTREGLER1:C4.2, 5V-SCHALTREGLER1:D1.2, 5V-SCHALTREGLER1:IC2.3
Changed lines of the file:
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@@
 <contactref element="PHOTOTRANSISTOR2:R15" pad="2"/>
 <contactref element="PHOTOTRANSISTOR2:R16" pad="2"/>
+<contactref element="ANSCHLUSS1:X1" pad="P$3"/>
 <wire x1="-980.35" y1="-282.88" x2="-987.97" y2="-282.88" width="0" layer="19" extent="1-1"/>
 <wire x1="-972.73" y1="-282.88" x2="-980.35" y2="-282.88" width="0" layer="19" extent="1-1"/>
@@
 <wire x1="-1159.3117" y1="-468.63" x2="-1160.5817" y2="-462.28" width="0" layer="19" extent="1-1"/>
 <wire x1="-1159.3117" y1="-474.98" x2="-1159.3117" y2="-468.63" width="0" layer="19" extent="1-1"/>
-<wire x1="-1247.4482" y1="-564.515" x2="-1166.9317" y2="-481.33" width="0" layer="19" extent="1-1"/>
+<wire x1="-1237.77" y1="-568.71" x2="-1166.9317" y2="-481.33" width="0" layer="19" extent="1-1"/>
+<wire x1="-1247.4482" y1="-564.515" x2="-1237.77" y2="-568.71" width="0" layer="19" extent="1-1"/>
 <wire x1="-1258.89" y1="-585.47" x2="-1247.4482" y2="-564.515" width="0" layer="19" extent="1-1"/>
 <wire x1="-1258.89" y1="-591.82" x2="-1258.89" y2="-585.47" width="0" layer="19" extent="1-1"/>
@@
 <contactref element="ARDUINO1:R4" pad="1"/>
 <contactref element="ARDUINO1:R4" pad="2"/>
+<contactref element="5V-SCHALTREGLER1:IC2" pad="3"/>
+<contactref element="5V-SCHALTREGLER1:C3" pad="2"/>
+<contactref element="5V-SCHALTREGLER1:C4" pad="2"/>
+<contactref element="5V-SCHALTREGLER1:D1" pad="2"/>
 <wire x1="-975.45" y1="-286.08" x2="-983.07" y2="-286.08" width="0" layer="19" extent="1-1"/>
 <wire x1="-967.83" y1="-286.08" x2="-975.45" y2="-286.08" width="0" layer="19" extent="1-1"/>
@@
 <wire x1="-1439.075" y1="-722.92" x2="-1438.59" y2="-716.28" width="0" layer="19" extent="1-1"/>
 <wire x1="-1431.125" y1="-722.92" x2="-1439.075" y2="-722.92" width="0" layer="19" extent="1-1"/>
+<wire x1="-24.13" y1="-9.75" x2="-609.2918" y2="-80.645" width="0" layer="19" extent="1-1"/>
+<wire x1="-12.71" y1="-3.81" x2="-24.13" y2="-9.75" width="0" layer="19" extent="1-1"/>
+<wire x1="-19.09" y1="7.62" x2="-12.71" y2="-3.81" width="0" layer="19" extent="1-1"/>
+<wire x1="-3.83" y1="6.35" x2="-12.71" y2="-3.81" width="0" layer="19" extent="1-1"/>
 </signal>
 <signal name="LED-IN">
@@
 <signal name="N$1">
 <contactref element="ANSCHLUSS1:X2" pad="P$6"/>
-</signal>
-<signal name="5V-SCHALTREGLER1:GND">
-<contactref element="5V-SCHALTREGLER1:IC2" pad="3"/>
-<contactref element="5V-SCHALTREGLER1:C3" pad="2"/>
-<contactref element="5V-SCHALTREGLER1:C4" pad="2"/>
-<contactref element="5V-SCHALTREGLER1:D1" pad="2"/>
-<wire x1="-12.71" y1="-3.81" x2="-24.13" y2="-9.75" width="0" layer="19" extent="1-1"/>
-<wire x1="-19.09" y1="7.62" x2="-12.71" y2="-3.81" width="0" layer="19" extent="1-1"/>
-<wire x1="-3.83" y1="6.35" x2="-12.71" y2="-3.81" width="0" layer="19" extent="1-1"/>
 </signal>
 <signal name="PHOTOTRANSISTOR2:N$1">
@@
 <wire x1="-1428.3287" y1="-674.44" x2="-609.2918" y2="-66.675" width="0" layer="19" extent="1-1"/>
 </signal>
-<signal name="ANSCHLUSS1:VID">
-<contactref element="ANSCHLUSS1:X1" pad="P$3"/>
-</signal>
 <signal name="N$10">

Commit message: + brd (layout)
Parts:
- moved PHOTOTRANSISTOR2:T9 1513.2 mm to (-10.0, 0.00)
- moved PHOTOTRANSISTOR2:T8 1493.8 mm to (0.00, -52.0), turned to 180 degrees
- moved PHOTOTRANSISTOR2:T7 1490.6 mm to (0.00, -46.0), turned to 180 degrees
- moved PHOTOTRANSISTOR2:T6 1487.5 mm to (0.00, -40.0), turned to 180 degrees
- moved PHOTOTRANSISTOR2:T5 1484.3 mm to (0.00, -34.0), turned to 180 degrees
- moved PHOTOTRANSISTOR2:T4 1481.3 mm to (0.00, -28.0), turned to 180 degrees
- moved PHOTOTRANSISTOR2:T3 1478.2 mm to (0.00, -22.0), turned to 180 degrees
- moved PHOTOTRANSISTOR2:T2 1475.2 mm to (0.00, -16.0), turned to 180 degrees
- moved PHOTOTRANSISTOR2:T1 1432.9 mm to (0.00, -10.0), turned to 180 degrees
- moved PHOTOTRANSISTOR2:T16 1430.9 mm to (-52.0, 0.00)
- moved PHOTOTRANSISTOR2:T15 1430.6 mm to (-46.0, 0.00)
- moved PHOTOTRANSISTOR2:T14 1430.3 mm to (-40.0, 0.00)
- moved PHOTOTRANSISTOR2:T13 1430.0 mm to (-34.0, 0.00)
- moved PHOTOTRANSISTOR2:T12 1429.7 mm to (-28.0, 0.00)
- moved PHOTOTRANSISTOR2:T11 1429.4 mm to (-22.0, 0.00)
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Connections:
- net RX: now also ANSCHLUSS1:X1.P$4, ARDUINO1:R1.2; no longer ANSCHLUSS1:X1.P$5, ARDUINO1:R2.2
- net TX: now also ANSCHLUSS1:X1.P$5, ARDUINO1:R2.2; no longer ANSCHLUSS1:X1.P$4, ARDUINO1:R1.2
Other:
- board size 160 x 100 mm -> 160 x 140 mm
